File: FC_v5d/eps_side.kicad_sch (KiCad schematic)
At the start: 67 parts, among them IC6 LT3652IMSE#PBF, J10 INHIBIT_P2, J11 DF11CZ-12DP-2V(27), J14 Battery Input, J17 Face4 (Z- Face), J19 ISS_INHIBIT, J2 DF11CZ-12DP-2V(27), J20 RBF_Inhibit, J21 Heater Output, J23 Aux Deploy 1, J24 Deploy 2, J29 INHIBIT_S2, J7 INHIBIT_P1, J8 INHIBIT_S1, U10 TPS54226PWPRPWP14_2P31X2P46-L, U13 TPS54225PWPR, U26 INA260, U3 INA260, U9 MCP23017_SS

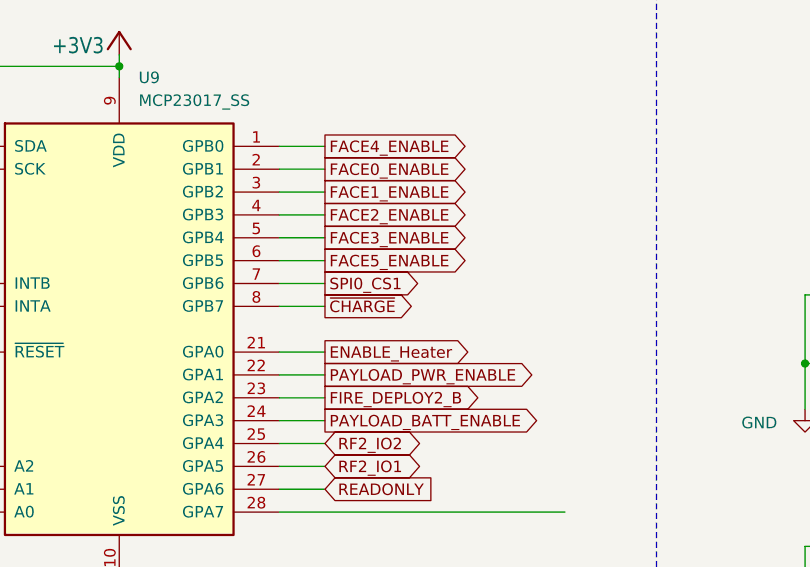
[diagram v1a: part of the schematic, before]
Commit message: Added Missing TCA4307 Pull Ups
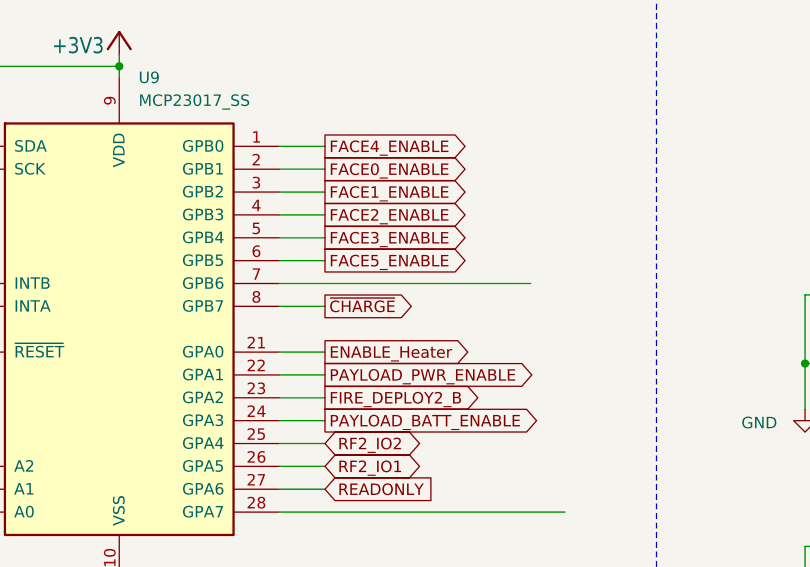
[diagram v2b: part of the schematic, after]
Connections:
- net SPI0_CS1: no longer names the net of U9.7 (GPB6)
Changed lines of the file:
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@@
 	(wire
 		(pts
-			(xy 91.44 240.03) (xy 86.36 240.03)
+			(xy 114.3 240.03) (xy 86.36 240.03)
 		)
 		(stroke
@@
 				(hide yes)
 			)
-		)
-	)
-	(global_label "SPI0_CS1"
-		(shape output)
-		(at 91.44 240.03 0)
-		(fields_autoplaced yes)
-		(effects
-			(font
-				(size 1.27 1.27)
-			)
-			(justify left)
-		)
-		(property "Intersheetrefs" "${INTERSHEET_REFS}"
-			(at 103.3756 240.03 0)
-			(effects
-				(font
-					(size 1.27 1.27)
-				)
-				(justify left)
-				(hide yes)
-			)

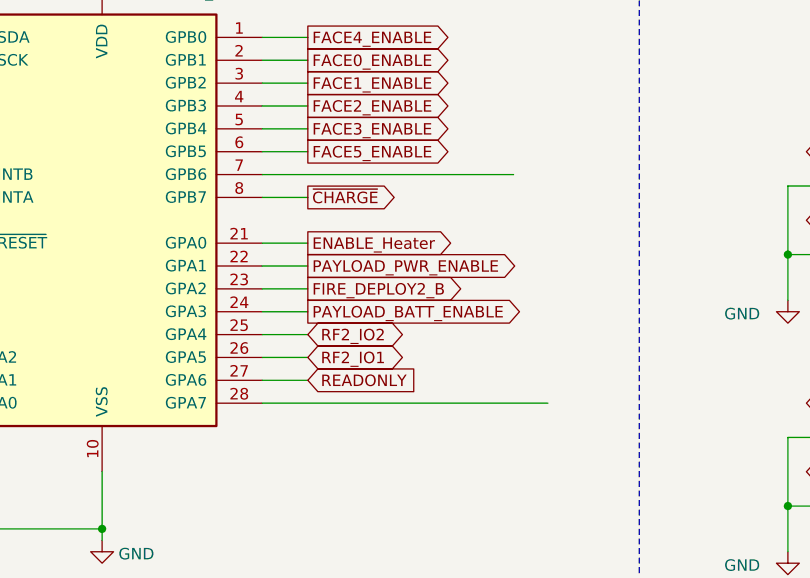
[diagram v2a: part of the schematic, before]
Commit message: Moved RF2IO to GPIO Expander
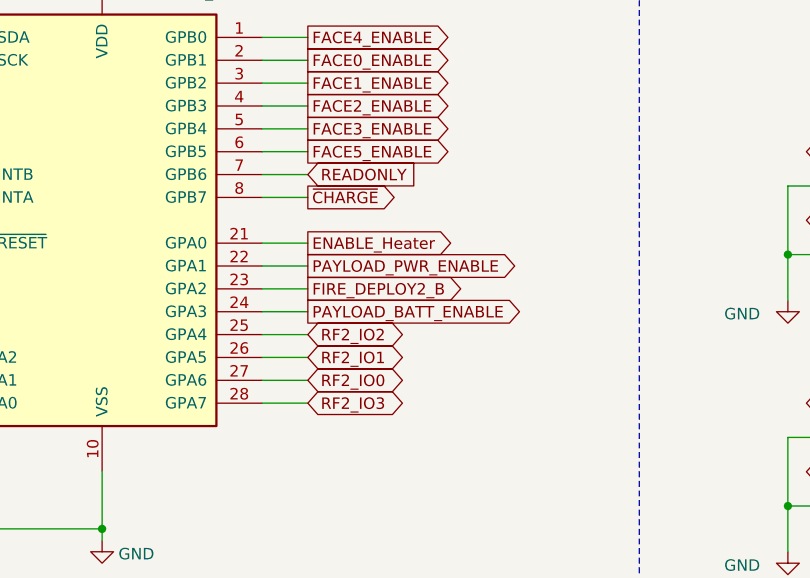
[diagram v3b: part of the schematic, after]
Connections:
- net READONLY: now also U9.7 (GPB6); no longer U9.27 (GPA6)
- net RF2_IO3: now reaches U9.28 (GPA7)
- new net RF2_IO0: U9.27 (GPA6)
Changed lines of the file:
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@@
 	(wire
 		(pts
-			(xy 86.36 265.43) (xy 118.11 265.43)
+			(xy 86.36 265.43) (xy 91.44 265.43)
 		)
 		(stroke
@@
 	(wire
 		(pts
-			(xy 114.3 240.03) (xy 86.36 240.03)
+			(xy 91.44 240.03) (xy 86.36 240.03)
 		)
 		(stroke
@@
 		)
 	)
+	(global_label "RF2_IO0"
+		(shape bidirectional)
+		(at 91.44 262.89 0)
+		(fields_autoplaced yes)
+		(effects
+			(font
+				(size 1.27 1.27)
+			)
+			(justify left)
+		)
+		(property "Intersheetrefs" "${INTERSHEET_REFS}"
+			(at 103.217 262.89 0)
+			(effects
+				(font
+					(size 1.27 1.27)
+				)
+				(justify left)
+				(hide yes)
+			)
+		)
+	)
 	(global_label "SCL1"
 		(shape bidirectional)
@@
 		)
 	)
+	(global_label "READONLY"
+		(shape input)
+		(at 91.44 240.03 0)
+		(fields_autoplaced yes)
+		(effects
+			(font
+				(size 1.27 1.27)
+			)
+			(justify left)
+		)
+		(property "Intersheetrefs" "${INTERSHEET_REFS}"
+			(at 103.9805 240.03 0)
+			(effects
+				(font
+					(size 1.27 1.27)
+				)
+				(justify left)
+				(hide yes)
+			)
+		)
+	)
 	(global_label "DEPLOY2"
 		(shape input)
@@
 		)
 	)
-	(global_label "GND"
+	(global_label "RF2_IO3"
 		(shape bidirectional)
-		(at 386.08 100.33 180)
+		(at 91.44 265.43 0)
 		(fields_autoplaced yes)
 		(effects
 			(font
-				(size 0.254 0.254)
+				(size 1.27 1.27)
 			)
-			(justify right)
+			(justify left)
 		)
 		(property "Intersheetrefs" "${INTERSHEET_REFS}"
-			(at 242.57 -91.44 0)
+			(at 103.217 265.43 0)
 			(effects
 				(font
 					(size 1.27 1.27)
 				)
+				(justify left)
 				(hide yes)
 			)
 		)
 	)
-	(global_label "READONLY"
-		(shape input)
-		(at 91.44 262.89 0)
+	(global_label "GND"
+		(shape bidirectional)
+		(at 386.08 100.33 180)
 		(fields_autoplaced yes)
 		(effects
 			(font
-				(size 1.27 1.27)
+				(size 0.254 0.254)
 			)
-			(justify left)
+			(justify right)
 		)
 		(property "Intersheetrefs" "${INTERSHEET_REFS}"
-			(at 103.9805 262.89 0)
+			(at 242.57 -91.44 0)
 			(effects
 				(font
 					(size 1.27 1.27)
 				)
-				(justify left)
 				(hide yes)
 			)

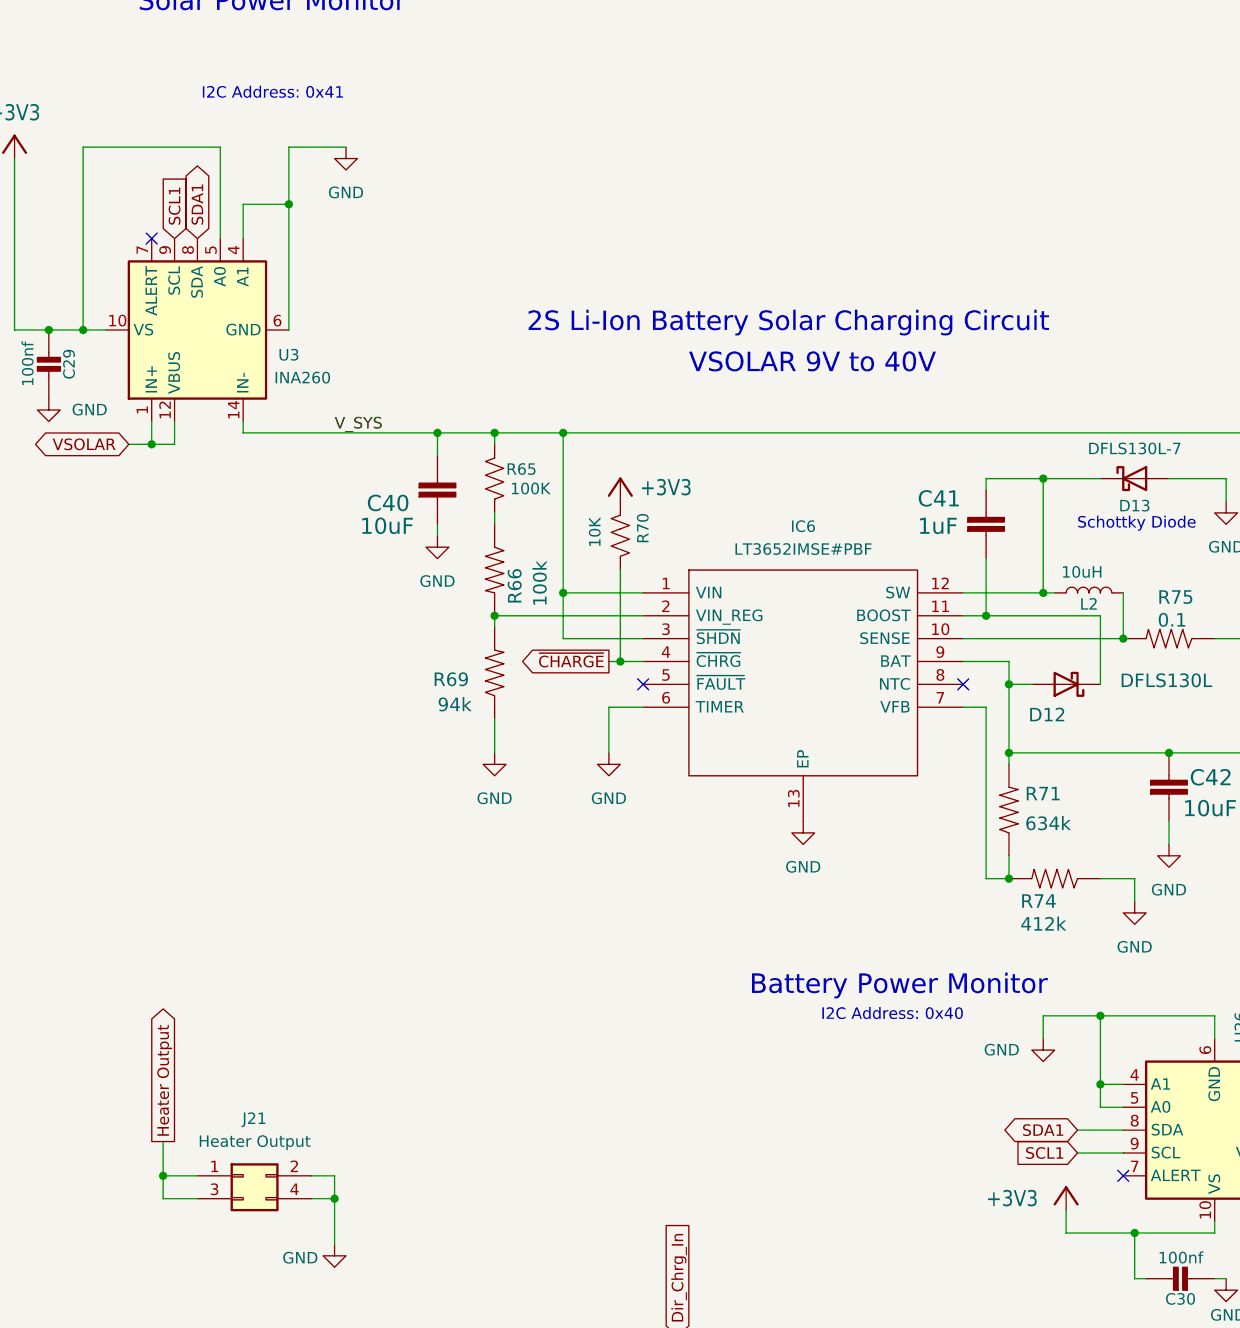
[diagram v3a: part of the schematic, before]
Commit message: Moved SDA0 and SCL0 to GP24 and GP25
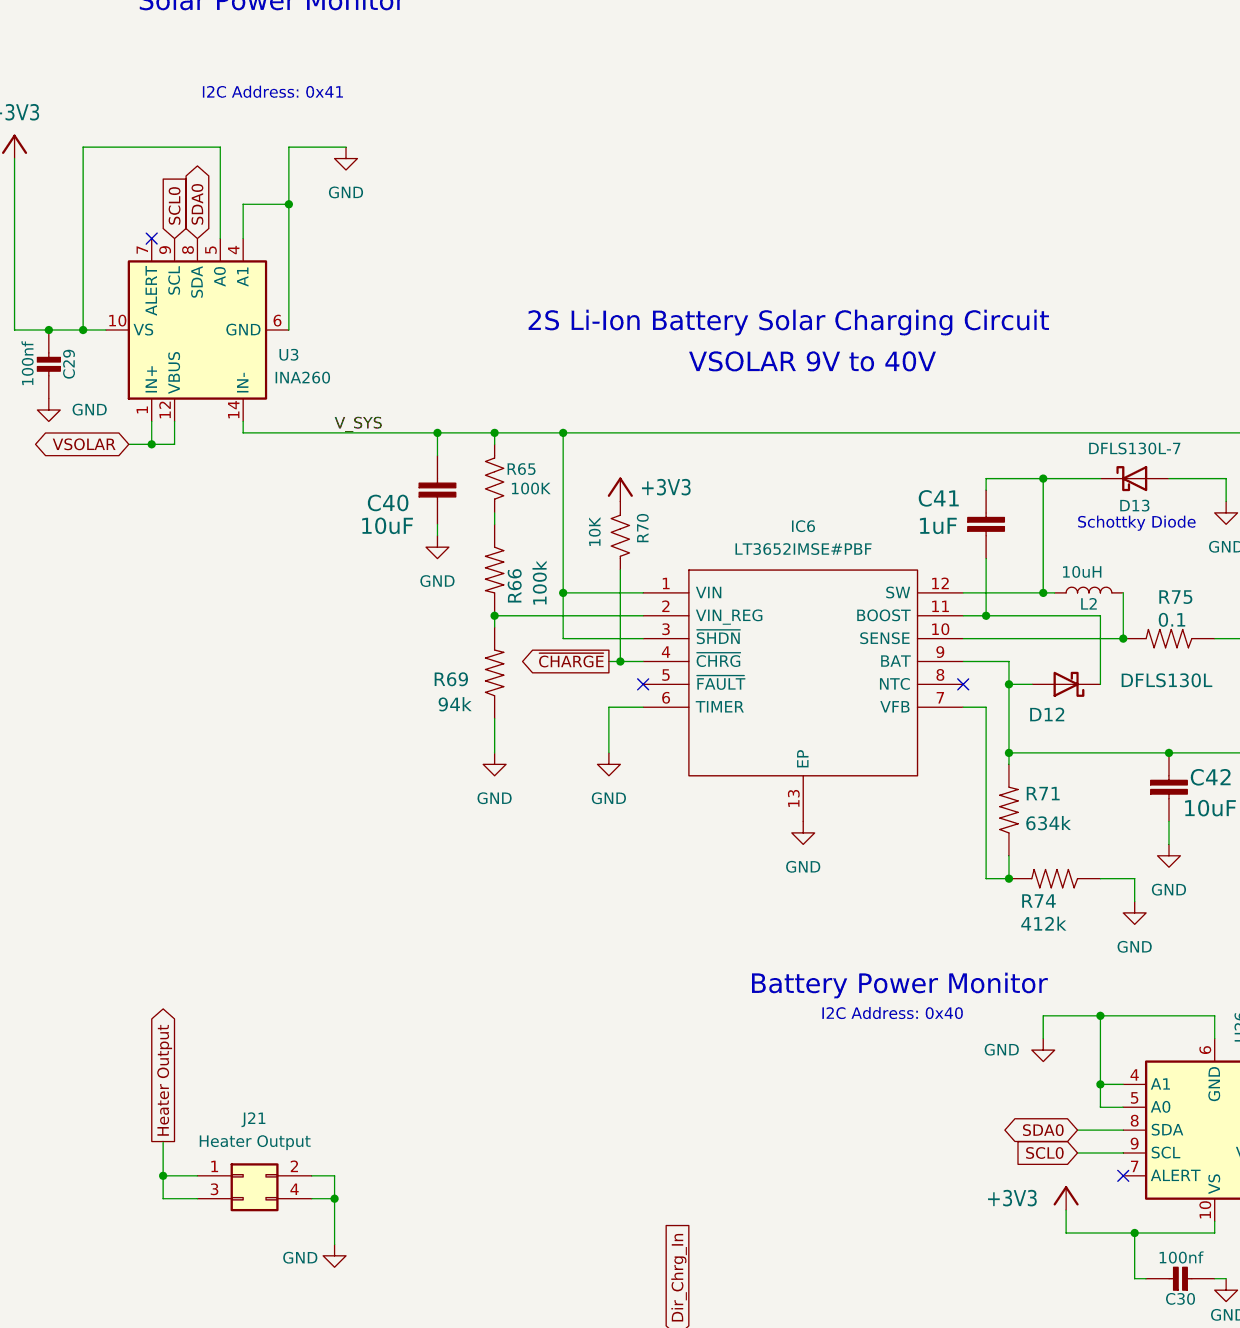
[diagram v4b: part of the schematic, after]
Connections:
- net SCL1: no longer U26.9 (SCL), U3.9 (SCL)
- net SDA1: no longer U26.8 (SDA), U3.8 (SDA)
- new net SCL0: U26.9 (SCL), U3.9 (SCL)
- new net SDA0: U26.8 (SDA), U3.8 (SDA)
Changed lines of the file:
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@@
 		)
 	)
-	(global_label "SDA1"
+	(global_label "SDA0"
 		(shape bidirectional)
 		(at 40.64 41.91 90)
@@
 		)
 	)
-	(global_label "SCL1"
+	(global_label "SCL0"
 		(shape input)
 		(at 38.1 41.91 90)
@@
 		)
 	)
-	(global_label "SCL1"
+	(global_label "SCL0"
 		(shape input)
 		(at 138.43 143.51 180)
@@
 		)
 	)
-	(global_label "SDA1"
+	(global_label "SDA0"
 		(shape bidirectional)
 		(at 138.43 140.97 180)
